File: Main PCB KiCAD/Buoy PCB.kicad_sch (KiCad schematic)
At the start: 2 parts

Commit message: PCB sub assembly
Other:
- added sheet Battery (battery.kicad_sch)
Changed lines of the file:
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@@
+	)
+	(sheet
+		(at 60.96 110.49)
+		(size 31.75 13.97)
+		(exclude_from_sim no)
+		(in_bom yes)
+		(on_board yes)
+		(dnp no)
+		(fields_autoplaced yes)
+		(stroke
+			(width 0.1524)
+			(type solid)
+		)
+		(fill
+			(color 0 0 0 0.0000)
+		)
+		(property "Sheetname" "Battery"
+			(at 60.96 109.7784 0)
+			(effects
+				(font
+					(size 1.27 1.27)
+				)
+				(justify left bottom)
+			)
+		)
+		(property "Sheetfile" "battery.kicad_sch"
+			(at 60.96 125.0446 0)
+			(effects
+				(font
+					(size 1.27 1.27)
+				)
+				(justify left top)
+				(hide yes)
+			)
+		)
+		(instances
+			(project "Buoy PCB"
+				(path "/a041e2a6-7d41-458c-91f3-753821d3dfe9"
+					(page "7")
+				)
+			)
+		)
 	)
 	(sheet

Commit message: battery charging
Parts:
- removed D10, D11: RB550VM-30TE-17, Diode_SMD:D_SOD-323_HandSoldering, symbol Device:D_Small_Filled
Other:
- removed sheet Battery

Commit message: clean
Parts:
- added J8: Conn_01x12_Pin, Connector_PinHeader_2.54mm:PinHeader_1x12_P2.54mm_Vertical, symbol Connector:Conn_01x12_Pin
- added J9: Conn_01x12_Socket, Connector_PinSocket_2.54mm:PinSocket_1x12_P2.54mm_Vertical, symbol Connector:Conn_01x12_Socket
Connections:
- net +Solar: now also J9.2 (Pin_2)
- net GND: now also J9.3 (Pin_3), J9.4 (Pin_4), J9.7 (Pin_7)
- new net +3.3V: J9.1 (Pin_1)
- new net +3.3V_bat: J8.1 (Pin_1)
- new net +Solar_Batt: J8.2 (Pin_2)
- new net GND_Batt: J8.3 (Pin_3), J8.4 (Pin_4), J8.7 (Pin_7)
- new net V_Batt_An: J8.5 (Pin_5)
- new net V_Solar_An: J8.6 (Pin_6)
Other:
- removed sheet CAN Interface
- sheet Battery Charger ports: added PG, Status1, Status2, V_Batt_An; removed none

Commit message: update
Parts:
- added J2: Conn_01x12_Socket, Connector_PinSocket_2.54mm:PinSocket_1x12_P2.54mm_Vertical, symbol Connector:Conn_01x12_Socket
- added J3: Conn_01x12_Pin, Connector_PinHeader_2.54mm:PinHeader_1x12_P2.54mm_Vertical, symbol Connector:Conn_01x12_Pin
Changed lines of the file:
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@@
+	(symbol
+		(lib_id "Connector:Conn_01x12_Pin")
+		(at 105.41 166.37 0)
+		(unit 1)
+		(exclude_from_sim no)
+		(in_bom yes)
+		(on_board yes)
+		(dnp no)
+		(fields_autoplaced yes)
+		(property "Reference" "J3"
+			(at 106.045 148.59 0)
+			(effects
+				(font
+					(size 1.27 1.27)
+				)
+			)
+		)
+		(property "Value" "Conn_01x12_Pin"
+			(at 106.045 151.13 0)
+			(effects
+				(font
+					(size 1.27 1.27)
+				)
+			)
+		)
+		(property "Footprint" "Connector_PinHeader_2.54mm:PinHeader_1x12_P2.54mm_Vertical"
+			(at 105.41 166.37 0)
+			(effects
+				(font
+					(size 1.27 1.27)
+				)
+				(hide yes)
+			)
+		)
+		(property "Datasheet" "~"
+			(at 105.41 166.37 0)
+			(effects
+				(font
+					(size 1.27 1.27)
+				)
+				(hide yes)
+			)
+		)
+		(property "Description" "Generic connector, single row, 01x12, script generated"
+			(at 105.41 166.37 0)
+			(effects
+				(font
+					(size 1.27 1.27)
+				)
+				(hide yes)
+			)
+		)
+		(pin "2"
+		)
+		(pin "5"
+		)
+		(pin "3"
+		)
+		(pin "8"
+		)
+		(pin "6"
+		)
+		(pin "11"
+		)
+		(pin "10"
+		)
+		(pin "7"
+		)
+		(pin "12"
+		)
+		(pin "4"
+		)
+		(pin "9"
+		)
+		(pin "1"
+		)
+		(instances
+			(project "Buoy PCB"
+				(path "/a041e2a6-7d41-458c-91f3-753821d3dfe9"
+					(reference "J3")
+					(unit 1)
+				)
+			)
+		)
+	)
+	(symbol
+		(lib_id "Connector:Conn_01x12_Socket")
+		(at 101.6 166.37 0)
+		(unit 1)
+		(exclude_from_sim no)
+		(in_bom yes)
+		(on_board yes)
+		(dnp no)
+		(fields_autoplaced yes)
+		(property "Reference" "J2"
+			(at 100.965 184.15 0)
+			(effects
+				(font
+					(size 1.27 1.27)
+				)
+			)
+		)
+		(property "Value" "Conn_01x12_Socket"
+			(at 100.965 186.69 0)
+			(effects
+				(font
+					(size 1.27 1.27)
+				)
+			)
+		)
+		(property "Footprint" "Connector_PinSocket_2.54mm:PinSocket_1x12_P2.54mm_Vertical"
+			(at 101.6 166.37 0)
+			(effects
+				(font
+					(size 1.27 1.27)
+				)
+				(hide yes)
+			)
+		)
+		(property "Datasheet" "~"
+			(at 101.6 166.37 0)
+			(effects
+				(font
+					(size 1.27 1.27)
+				)
+				(hide yes)
+			)
+		)
+		(property "Description" "Generic connector, single row, 01x12, script generated"
+			(at 101.6 166.37 0)
+			(effects
+				(font
+					(size 1.27 1.27)
+				)
+				(hide yes)
+			)
+		)
+		(pin "10"
+		)
+		(pin "12"
+		)
+		(pin "8"
+		)
+		(pin "11"
+		)
+		(pin "3"
+		)
+		(pin "6"
+		)
+		(pin "4"
+		)
+		(pin "1"
+		)
+		(pin "5"
+		)
+		(pin "7"
+		)
+		(pin "2"
+		)
+		(pin "9"
+		)
+		(instances
+			(project "Buoy PCB"
+				(path "/a041e2a6-7d41-458c-91f3-753821d3dfe9"
+					(reference "J2")
+					(unit 1)
+				)
+			)
+		)
+	)
 	(symbol
 		(lib_id "Connector:Conn_01x12_Pin")

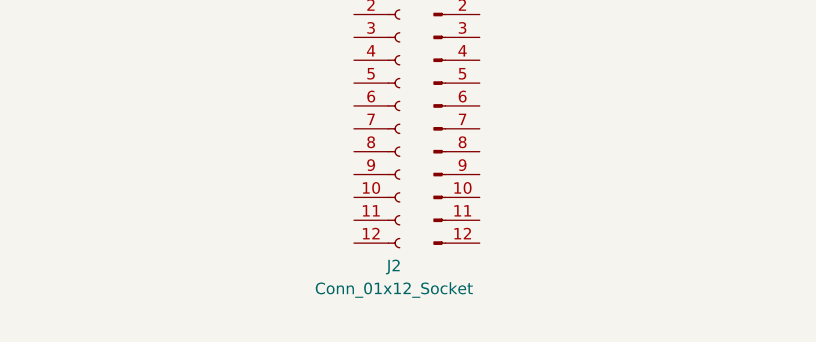
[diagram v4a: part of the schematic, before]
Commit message: moved connector
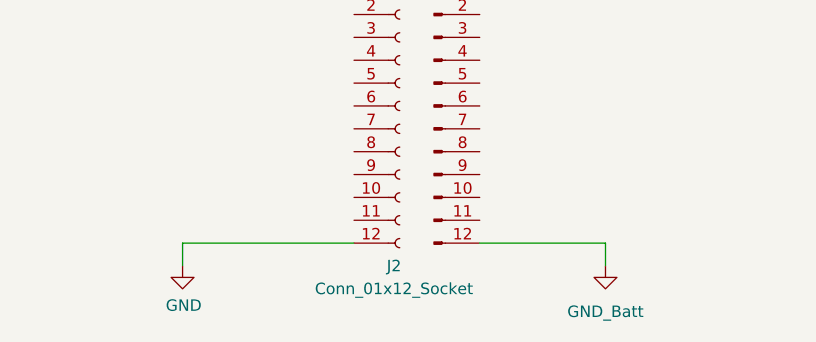
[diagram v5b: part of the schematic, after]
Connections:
- net GND: now also J2.12 (Pin_12)
- net GND_Batt: now also J3.12 (Pin_12)
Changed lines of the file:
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@@
+	(wire
+		(pts
+			(xy 124.46 184.15) (xy 124.46 181.61)
+		)
+		(stroke
+			(width 0)
+			(type default)
+		)
+	)
 	(wire
 		(pts
@@
 	(wire
 		(pts
+			(xy 77.47 181.61) (xy 77.47 184.15)
+		)
+		(stroke
+			(width 0)
+			(type default)
+		)
+	)
+	(wire
+		(pts
+			(xy 96.52 181.61) (xy 77.47 181.61)
+		)
+		(stroke
+			(width 0)
+			(type default)
+		)
+	)
+	(wire
+		(pts
 			(xy 110.49 118.11) (xy 124.46 118.11)
+		)
+		(stroke
+			(width 0)
+			(type default)
+		)
+	)
+	(wire
+		(pts
+			(xy 124.46 181.61) (xy 110.49 181.61)
 		)
 		(stroke
@@
 					(unit 1)
 				)
+			)
+		)
+	)
+	(symbol
+		(lib_id "power:GND")
+		(at 77.47 184.15 0)
+		(unit 1)
+		(exclude_from_sim no)
+		(in_bom yes)
+		(on_board yes)
+		(dnp no)
+		(property "Reference" "#PWR018"
+			(at 77.47 190.5 0)
+			(effects
+				(font
+					(size 1.27 1.27)
+				)
+				(hide yes)
+			)
+		)
+		(property "Value" "GND"
+			(at 77.597 188.5442 0)
+			(effects
+				(font
+					(size 1.27 1.27)
+				)
+			)
+		)
+		(property "Footprint" ""
+			(at 77.47 184.15 0)
+			(effects
+				(font
+					(size 1.27 1.27)
+				)
+				(hide yes)
+			)
+		)
+		(property "Datasheet" ""
+			(at 77.47 184.15 0)
+			(effects
+				(font
+					(size 1.27 1.27)
+				)
+				(hide yes)
+			)
+		)
+		(property "Description" ""
+			(at 77.47 184.15 0)
+			(effects
+				(font
+					(size 1.27 1.27)
+				)
+			)
+		)
+		(pin "1"
+		)
+		(instances
+			(project "Buoy PCB"
+				(path "/a041e2a6-7d41-458c-91f3-753821d3dfe9"
+					(reference "#PWR018")
+					(unit 1)
+				)
+			)
+		)
+	)
+	(symbol
+		(lib_id "power:GND")
+		(at 124.46 184.15 0)
+		(unit 1)
+		(exclude_from_sim no)
+		(in_bom yes)
+		(on_board yes)
+		(dnp no)
+		(fields_autoplaced yes)
+		(property "Reference" "#PWR020"
+			(at 124.46 190.5 0)
+			(effects
+				(font
+					(size 1.27 1.27)
+				)
+				(hide yes)
+			)
+		)
+		(property "Value" "GND_Batt"
+			(at 124.46 189.23 0)
+			(effects
+				(font
+					(size 1.27 1.27)
+				)
+			)
+		)
+		(property "Footprint" ""
+			(at 124.46 184.15 0)
+			(effects
+				(font
+					(size 1.27 1.27)
+				)
+				(hide yes)
+			)
+		)
+		(property "Datasheet" ""
+			(at 124.46 184.15 0)
+			(effects
+				(font
+					(size 1.27 1.27)
+				)
+				(hide yes)
+			)
+		)
+		(property "Description" "Power symbol creates a global label with name \"GND\" , ground"
+			(at 124.46 184.15 0)
+			(effects
+				(font
+					(size 1.27 1.27)
+				)
+				(hide yes)
+			)
+		)
+		(pin "1"
+		)
+		(instances
+			(project "Buoy PCB"
+				(path "/a041e2a6-7d41-458c-91f3-753821d3dfe9"
+					(reference "#PWR020")
+					(unit 1)
+				)

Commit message: updates
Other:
- sheet Squid: file squid.kicad_sch -> Assets/SubPCBs/Shrimps/Shrimp ATmega328P-P.kicad_sch
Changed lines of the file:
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@@
 	)
 	(sheet
-		(at 114.3 20.32)
+		(at 130.81 39.37)
 		(size 29.21 29.21)
 		(exclude_from_sim no)
@@
 		)
 		(property "Sheetname" "Squid"
-			(at 114.3 19.6084 0)
+			(at 130.81 38.6584 0)
 			(effects
 				(font
@@
 			)
 		)
-		(property "Sheetfile" "squid.kicad_sch"
-			(at 114.3 50.1146 0)
+		(property "Sheetfile" "Assets/SubPCBs/Shrimps/Shrimp ATmega328P-P.kicad_sch"
+			(at 130.81 69.1646 0)
 			(effects
 				(font

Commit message: update
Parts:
- renumbered J9 to J1, J8 to J3, J3 to J4
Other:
- added sheet Top PCB (Top.kicad_sch)
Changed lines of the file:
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@@
 		(dnp no)
 		(fields_autoplaced yes)
-		(property "Reference" "#PWR026"
+		(property "Reference" "#PWR01"
 			(at 31.75 41.91 0)
 			(effects
@@
 			(project "modbus sensor"
 				(path "/a041e2a6-7d41-458c-91f3-753821d3dfe9"
-					(reference "#PWR026")
+					(reference "#PWR01")
 					(unit 1)
 				)
@@
 		(dnp no)
 		(fields_autoplaced yes)
-		(property "Reference" "#PWR032"
+		(property "Reference" "#PWR08"
 			(at 113.03 104.14 0)
 			(effects
@@
 			(project "Buoy PCB"
 				(path "/a041e2a6-7d41-458c-91f3-753821d3dfe9"
-					(reference "#PWR032")
+					(reference "#PWR08")
 					(unit 1)
 				)
@@
 		(dnp no)
 		(fields_autoplaced yes)
-		(property "Reference" "#PWR041"
+		(property "Reference" "#PWR07"
 			(at 91.44 104.14 0)
 			(effects
@@
 			(project "Buoy PCB"
 				(path "/a041e2a6-7d41-458c-91f3-753821d3dfe9"
-					(reference "#PWR041")
+					(reference "#PWR07")
 					(unit 1)
 				)
@@
 		(dnp no)
 		(fields_autoplaced yes)
-		(property "Reference" "#PWR027"
+		(property "Reference" "#PWR03"
 			(at 36.83 31.75 0)
 			(effects
@@
 			(project "Buoy PCB"
 				(path "/a041e2a6-7d41-458c-91f3-753821d3dfe9"
-					(reference "#PWR027")
+					(reference "#PWR03")
 					(unit 1)
 				)
@@
 		(dnp no)
 		(fields_autoplaced yes)
-		(property "Reference" "J3"
+		(property "Reference" "J4"
 			(at 106.045 148.59 0)
 			(effects
@@
 			(project "Buoy PCB"
 				(path "/a041e2a6-7d41-458c-91f3-753821d3dfe9"
-					(reference "J3")
+					(reference "J4")
 					(unit 1)
 				)
@@
 		(on_board yes)
 		(dnp no)
-		(property "Reference" "#PWR018"
+		(property "Reference" "#PWR06"
 			(at 77.47 190.5 0)
 			(effects
@@
 			(project "Buoy PCB"
 				(path "/a041e2a6-7d41-458c-91f3-753821d3dfe9"
-					(reference "#PWR018")
+					(reference "#PWR06")
 					(unit 1)
 				)
@@
 		(dnp no)
 		(fields_autoplaced yes)
-		(property "Reference" "#PWR020"
+		(property "Reference" "#PWR011"
 			(at 124.46 190.5 0)
 			(effects
@@
 			(project "Buoy PCB"
 				(path "/a041e2a6-7d41-458c-91f3-753821d3dfe9"
-					(reference "#PWR020")
+					(reference "#PWR011")
 					(unit 1)
 				)
@@
 		(dnp no)
 		(fields_autoplaced yes)
-		(property "Reference" "J8"
+		(property "Reference" "J3"
 			(at 106.045 97.79 0)
 			(effects
@@
 			(project ""
 				(path "/a041e2a6-7d41-458c-91f3-753821d3dfe9"
-					(reference "J8")
+					(reference "J3")
 					(unit 1)
 				)
@@
 		(on_board yes)
 		(dnp no)
-		(property "Reference" "#PWR044"
+		(property "Reference" "#PWR05"
 			(at 77.47 139.7 0)
 			(effects
@@
 			(project "Buoy PCB"
 				(path "/a041e2a6-7d41-458c-91f3-753821d3dfe9"
-					(reference "#PWR044")
+					(reference "#PWR05")
 					(unit 1)
 				)
@@
 		(dnp no)
 		(fields_autoplaced yes)
-		(property "Reference" "#PWR034"
+		(property "Reference" "#PWR09"
 			(at 124.46 104.14 0)
 			(effects
@@
 			(project "Buoy PCB"
 				(path "/a041e2a6-7d41-458c-91f3-753821d3dfe9"
-					(reference "#PWR034")
+					(reference "#PWR09")
 					(unit 1)
 				)
@@
 		(dnp no)
 		(fields_autoplaced yes)
-		(property "Reference" "#PWR028"
+		(property "Reference" "#PWR02"
 			(at 36.83 34.29 0)
 			(effects
@@
 			(project "Buoy PCB"
 				(path "/a041e2a6-7d41-458c-91f3-753821d3dfe9"
-					(reference "#PWR028")
+					(reference "#PWR02")
 					(unit 1)
 				)
@@
 		(dnp no)
 		(fields_autoplaced yes)
-		(property "Reference" "#PWR043"
+		(property "Reference" "#PWR010"
 			(at 124.46 139.7 0)
 			(effects
@@
 			(project "Buoy PCB"
 				(path "/a041e2a6-7d41-458c-91f3-753821d3dfe9"
-					(reference "#PWR043")
+					(reference "#PWR010")
 					(unit 1)
 				)
@@
 		(dnp no)
 		(fields_autoplaced yes)
-		(property "Reference" "#PWR040"
+		(property "Reference" "#PWR04"
 			(at 77.47 104.14 0)
 			(effects
@@
 			(project "Buoy PCB"
 				(path "/a041e2a6-7d41-458c-91f3-753821d3dfe9"
-					(reference "#PWR040")
+					(reference "#PWR04")
 					(unit 1)
 				)
@@
 		(dnp no)
 		(fields_autoplaced yes)
-		(property "Reference" "J9"
+		(property "Reference" "J1"
 			(at 100.965 133.35 0)
 			(effects
@@
 			(project ""
 				(path "/a041e2a6-7d41-458c-91f3-753821d3dfe9"
-					(reference "J9")
+					(reference "J1")
 					(unit 1)
 				)
@@
 			)
 		)
+		(instances
+			(project "Buoy PCB"
+				(path "/a041e2a6-7d41-458c-91f3-753821d3dfe9"
+					(page "6")
+				)
+			)
+		)
+	)
+	(sheet
+		(at 312.42 95.25)
+		(size 34.29 35.56)
+		(exclude_from_sim no)
+		(in_bom yes)
+		(on_board yes)
+		(dnp no)
+		(fields_autoplaced yes)
+		(stroke
+			(width 0.1524)
+			(type solid)
+		)
+		(fill
+			(color 0 0 0 0.0000)
+		)
+		(property "Sheetname" "Top PCB"
+			(at 312.42 94.5384 0)
+			(effects
+				(font
+					(size 1.27 1.27)
+				)
+				(justify left bottom)
+			)
+		)
+		(property "Sheetfile" "Top.kicad_sch"
+			(at 312.42 131.3946 0)
+			(effects
+				(font
+					(size 1.27 1.27)
+				)
+				(justify left top)
+				(hide yes)
+			)
+		)
